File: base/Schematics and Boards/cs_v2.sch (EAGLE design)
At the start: 51 parts, among them J1 DM3AT-SF-PEJM5, Q1 DMG3415UFY4Q-7, U1 ATSAMD51, U2 MAX77827BEWC+T, U202 COULOMB-MAX17262, U206 LOADSWITCH-MIC94162, U3 PD3S140-7, Y1 16M, Y2 ABS07-32.768KHZ-9-T

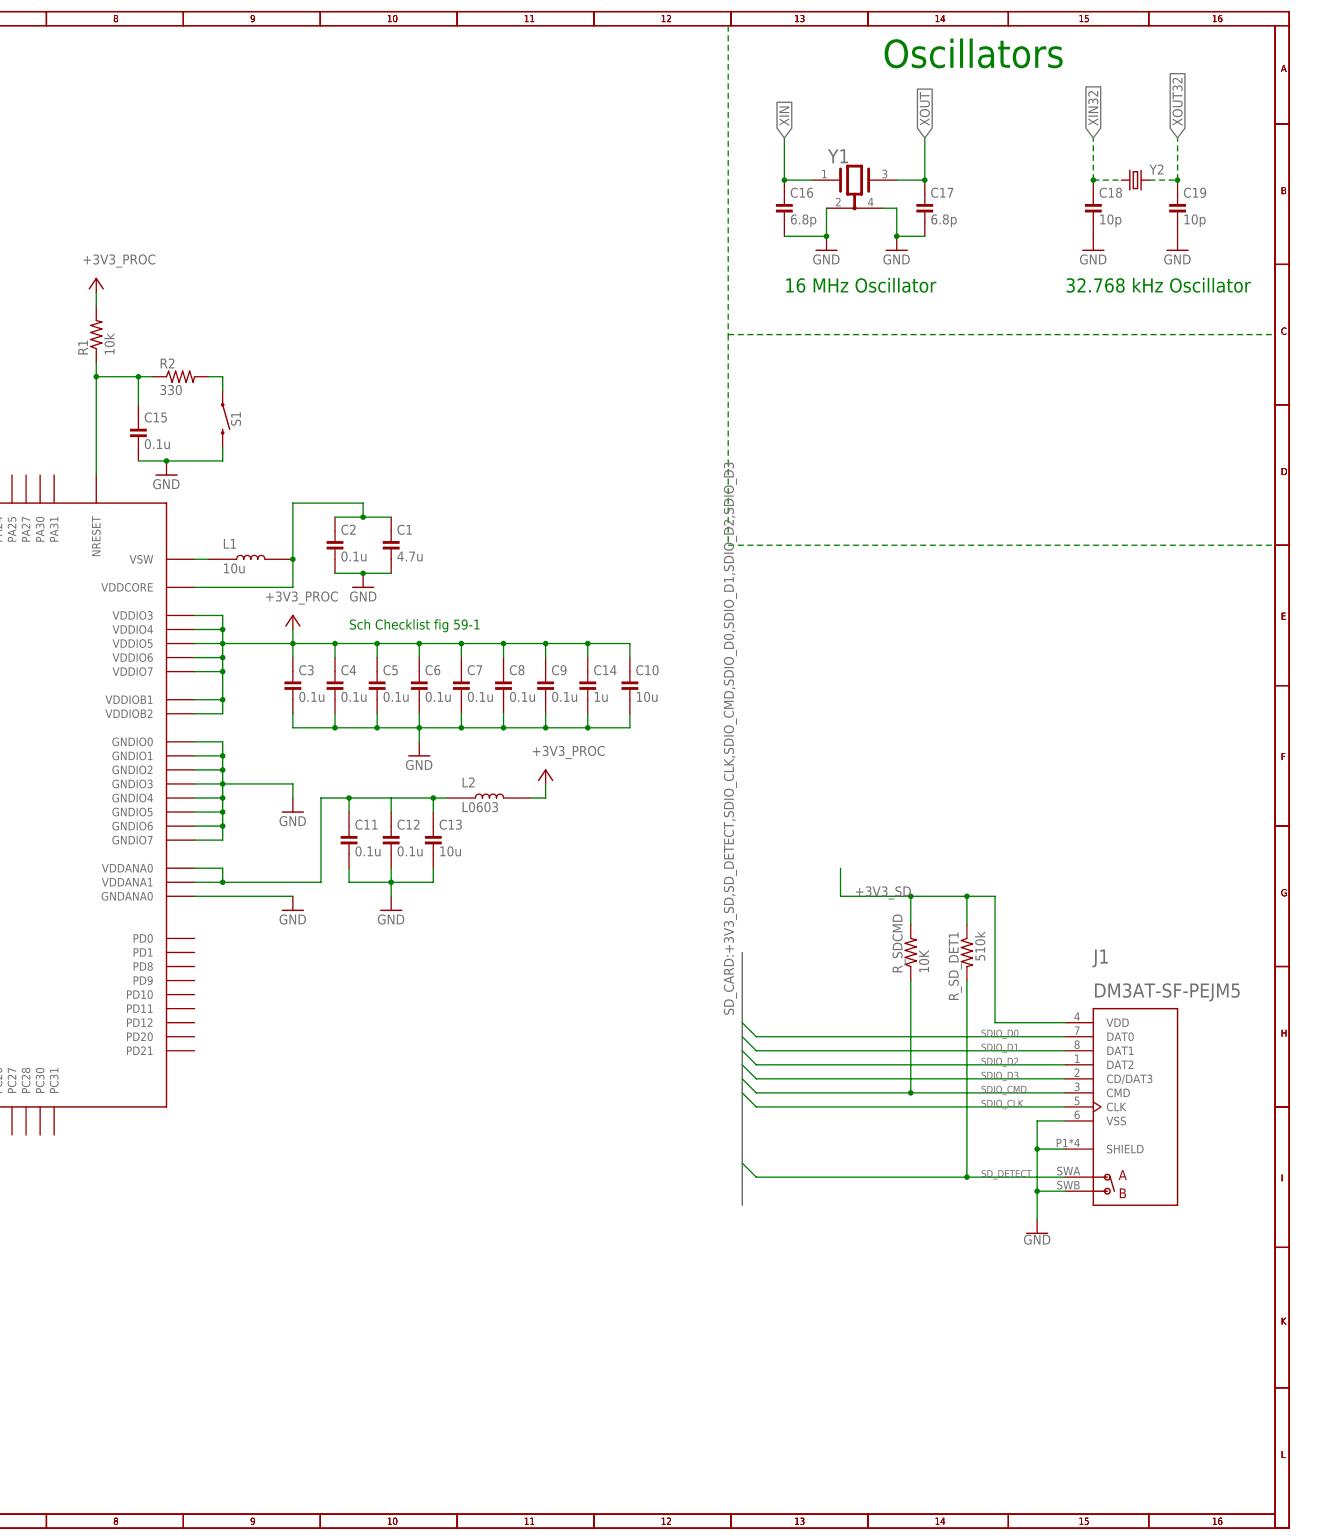
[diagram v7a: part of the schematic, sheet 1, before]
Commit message: Add indicator LEDs
LEDs powered by processor, but the processor cannot handle that much. Need MOSFET whose gates are connected to processor
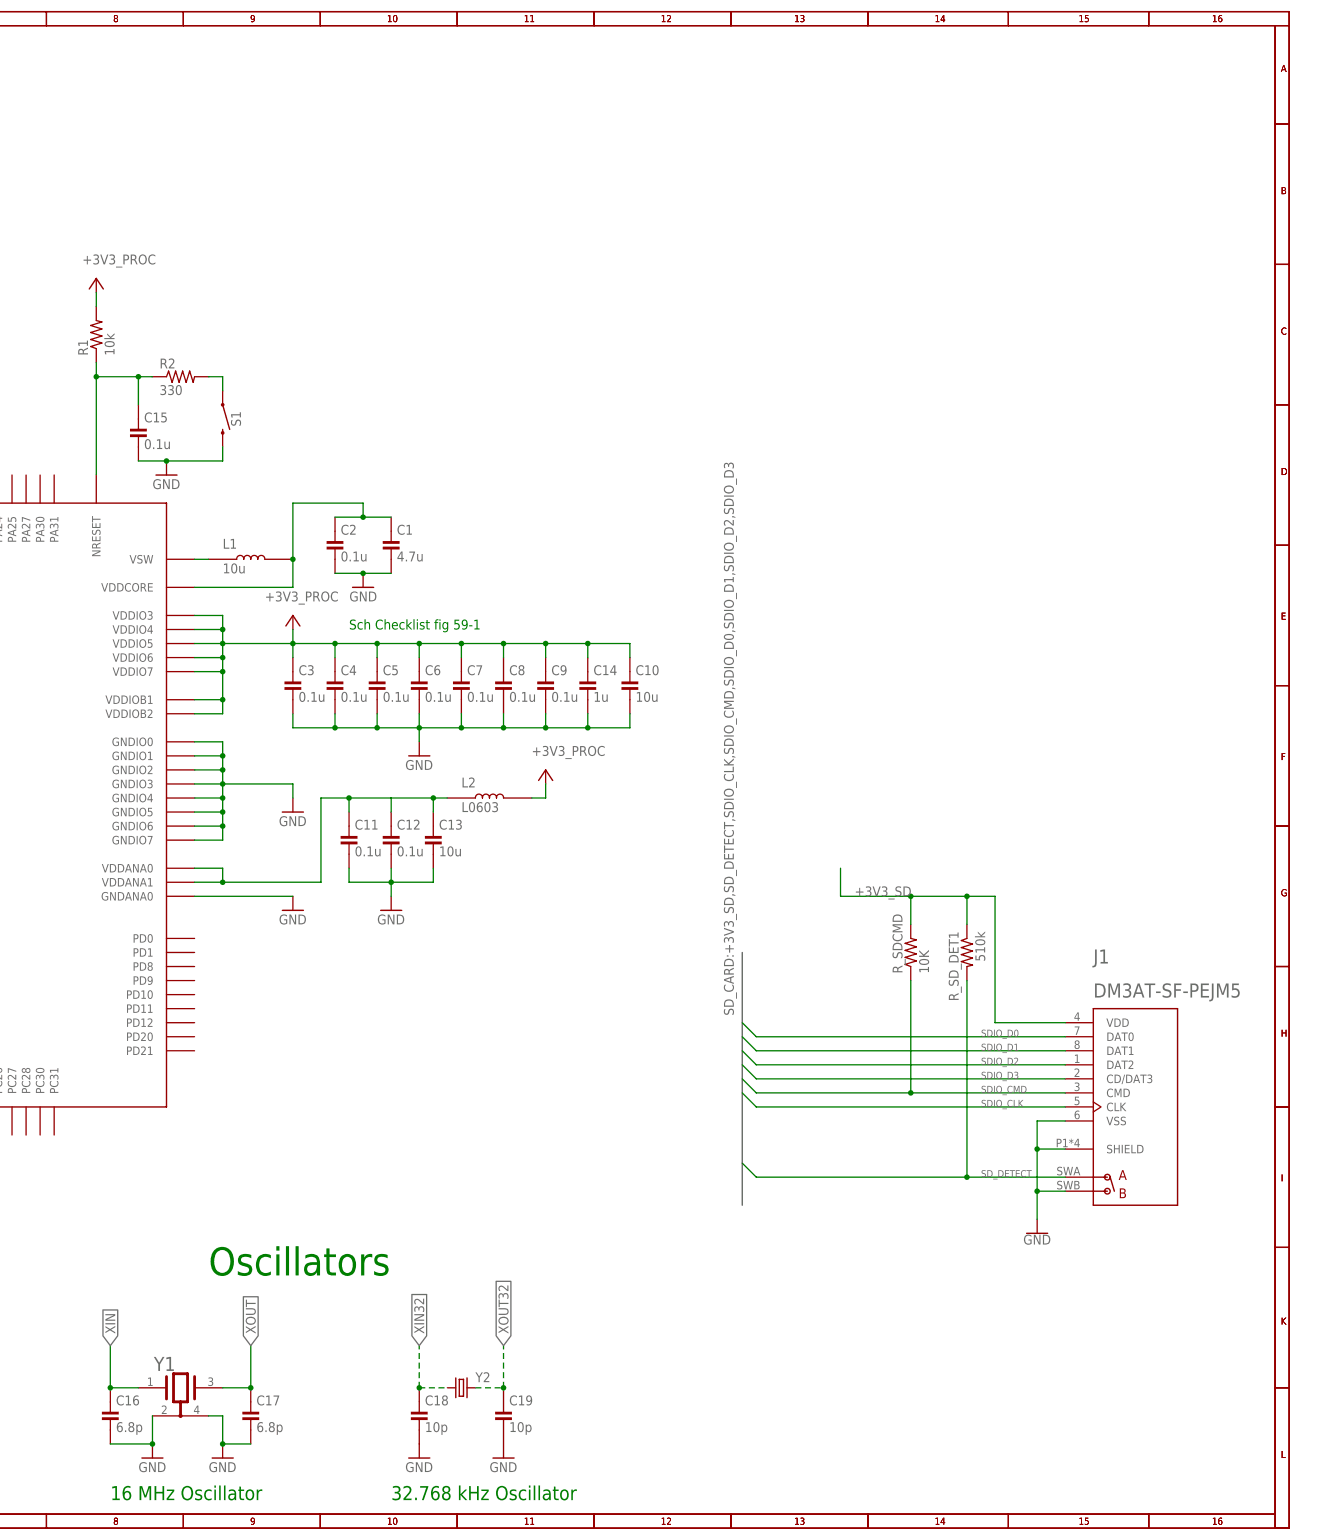
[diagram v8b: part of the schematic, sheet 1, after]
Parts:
- added D1: DIALIGHT_RGBLED_598-8710-307FDIALIGHT_598-8710-307F_0_0, Diodes:DIALIGHT_RGBLED_598-8710-307FDIALIGHT_598-8710-307F_0_0
- added R5: 150, Resistors:R-0402
- added R6, R7: 30, Resistors:R-0402
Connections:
- new net LED_B: R6.2
- new net LED_G: R7.2
- new net LED_R: R5.2
- new net N$12: D1.GREEN_CATHODE, R5.1
- new net N$14: D1.RED_CATHODE, R7.1
- new net N$4: D1.BLUE_CATHODE, R6.1
- net +3V3_PROC: now also D1.COMMON_ANODE
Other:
- note added: "Aim for 10 mA output for each LED. Green (1) and Blue(3) have forward biases near 3V, so no resistor needed. Red (2) has forward bias 1.8V. Outputs of this should be tied to GND by processor to turn an LED on."
- note added: "Indicator LEDs"
- note added: "PowerDue uses MOSFETs to rather than pins directly to processor. Should that be done again? It was used to segregate CPU and actuator rails"
- moved on the sheet: C16, C17, C18, C19, Y1, Y2
